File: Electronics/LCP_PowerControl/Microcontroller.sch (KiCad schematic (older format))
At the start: 20 parts, among them J4 Conn_02x02_Odd_Even, J5 Conn_02x05_Odd_Even, J6 Conn_02x06_Odd_Even, J7 Conn_02x02_Odd_Even, J8 Conn_02x02_Odd_Even, SW1 SW_Push, U3 MSP430FR5989, Y1 32.768kHz

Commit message: Adding libraries and recent changes
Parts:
- added RN? (x2): R_Pack02, symbol Device:R_Pack02
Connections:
- net +3V3: now also RN?.3 (R2.2), RN?.3 (R2.2), RN?.4 (R1.2), RN?.4 (R1.2)
- net BM_SCL: now also RN?.2 (R2.1)
- net BM_SDA: now also RN?.1 (R1.1)
- net CONTROL_SCL: now also RN?.2 (R2.1)
- net CONTROL_SDA: now also RN?.1 (R1.1)
- net HALL_EFFECT_CH_A renamed ENCODER_CH_A
- net HALL_EFFECT_CH_B renamed ENCODER_CH_B
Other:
- moved on the sheet: C10, C11, C12, C13, C14, C15, C16, C8, C9, J5, J6, JP1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

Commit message: Aiming for rev 0.1 complete
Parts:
- C16: value 1n -> 1000pF; footprint (none) -> Capacitor_SMD:C_0603_1608Metric
- J4, J7, J8: footprint (none) -> Connector_PinHeader_2.00mm:PinHeader_2x02_P2.00mm_Vertical
- J5: footprint (none) -> Connector_PinSocket_1.27mm:PinSocket_2x05_P1.27mm_Vertical
- J6: footprint (none) -> Connector_PinHeader_2.00mm:PinHeader_2x06_P2.00mm_Vertical
- JP1, JP2: footprint (none) -> Jumper:SolderJumper-2_P1.3mm_Bridged_RoundedPad1.0x1.5mm
- R13: footprint (none) -> Resistor_SMD:R_0805_2012Metric
- RN1, RN2: renamed from RN?; footprint (none) -> Resistor_SMD:R_Array_Concave_2x0603; MPN (none) -> EXB-V4V472JV
- SW1: footprint (none) -> Button_Switch_SMD:SW_SPST_TL3305A; MPN (none) -> PTS810 SJS 250 SMTR LFS
- Y1: footprint (none) -> Crystal:Crystal_SMD_HC49-SD
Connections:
- net P5.3: now reaches U3.13 (P5.3/UDB1STE)
- net P1.4: now reaches U3.2 (P1.4/UCB0CLK/UCA0STE/TA1.0)
- net P3.3: now reaches U3.25 (P3.3/TA1.1/TB0CLK)
- net P2.3: now reaches U3.30 (P2.3/UCA0STE/TB0OUTH)
- net P2.2: now reaches U3.31 (P2.2/UCA0CLK/TB0.4/RTCCLK)
- net P1.3: now reaches U3.36 (P1.3/ESITEST4/TA1.2/A3/C3)
- net P2.6: now reaches U3.8 (P2.6/TB0.5/ESIC1OUT)
- net P2.7: now reaches U3.9 (P2.7/TB0.6/ESIC2OUT)
- no-connect marks 8 -> 13
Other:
- note added: "Unused Nets"
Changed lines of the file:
@@
 Sheet 8 11
 Title ""
-Date ""
-Rev ""
+Date "2020-06-17"
+Rev "R0.1"
 Comp ""
-Comment1 ""
+Comment1 "Design by: Matt Casari"
 Comment2 ""
 Comment3 ""
@@
 Text HLabel 15050 4000 2    50   Output ~ 0
 ~MD_SLEEP
-Text HLabel 3900 8550 0    50   Output ~ 0
+Text HLabel 3900 5550 0    50   Output ~ 0
 12V_ENABLE
 $Comp
@@
 U 1 1 5EE55967
 P 8300 4750
-F 0 "U3" H 8275 7281 50  0000 C CNN
-F 1 "MSP430FR5989" H 8275 7190 50  0000 C CNN
+F 0 "U3" H 9750 7050 50  0000 C CNN
+F 1 "MSP430FR5989" H 7100 7050 50  0000 C CNN
 F 2 "Package_QFP:LQFP-64_10x10mm_P0.5mm" H 7700 6450 50  0001 C CNN
 F 3 "https://www.ti.com/lit/ds/symlink/msp430fr5989.pdf?ts=1591995725922&ref_url=https%253A%252F%252Fwww.ti.com%252Fproduct%252FMSP430FR5989" H 7700 6450 50  0001 C CNN
@@
 F 0 "JP1" H 8300 7400 50  0000 C CNN
 F 1 "SolderJumper_2_Bridged" H 8300 7000 50  0001 C CNN
-F 2 "" H 8300 7300 50  0001 C CNN
+F 2 "Jumper:SolderJumper-2_P1.3mm_Bridged_RoundedPad1.0x1.5mm" H 8300 7300 50  0001 C CNN
 F 3 "~" H 8300 7300 50  0001 C CNN
 	1    8300 7300
@@
 F 0 "J5" V 11459 2580 50  0000 L CNN
 F 1 "Conn_02x05_Odd_Even" V 11550 2580 50  0000 L CNN
-F 2 "" H 11500 2300 50  0001 C CNN
+F 2 "Connector_PinSocket_1.27mm:PinSocket_2x05_P1.27mm_Vertical" H 11500 2300 50  0001 C CNN
 F 3 "~" H 11500 2300 50  0001 C CNN
 F 4 "JTAG_MINI" V 11641 2580 50  0000 L CNN "Field4"
@@
 F 0 "Y1" V 10054 6631 50  0000 L CNN
 F 1 "32.768kHz" V 10145 6631 50  0000 L CNN
-F 2 "" H 10100 6500 50  0001 C CNN
+F 2 "Crystal:Crystal_SMD_HC49-SD" H 10100 6500 50  0001 C CNN
 F 3 "~" H 10100 6500 50  0001 C CNN
 	1    10100 6500
@@
 F 0 "R13" H 12220 3346 50  0000 L CNN
 F 1 "470" H 12220 3255 50  0000 L CNN
-F 2 "" V 12080 3300 50  0001 C CNN
+F 2 "Resistor_SMD:R_0805_2012Metric" V 12080 3300 50  0001 C CNN
 F 3 "~" H 12150 3300 50  0001 C CNN
 	1    12150 3300
@@
 P 12150 3700
 F 0 "C16" H 12265 3746 50  0000 L CNN
-F 1 "1n" H 12265 3655 50  0000 L CNN
-F 2 "" H 12188 3550 50  0001 C CNN
+F 1 "1000pF" H 12265 3655 50  0000 L CNN
+F 2 "Capacitor_SMD:C_0603_1608Metric" H 12188 3550 50  0001 C CNN
 F 3 "~" H 12150 3700 50  0001 C CNN
 	1    12150 3700
@@
 F 0 "SW1" H 12650 3785 50  0000 C CNN
 F 1 "SW_Push" H 12650 3694 50  0000 C CNN
-F 2 "" H 12650 3700 50  0001 C CNN
+F 2 "Button_Switch_SMD:SW_SPST_TL3305A" H 12650 3700 50  0001 C CNN
 F 3 "~" H 12650 3700 50  0001 C CNN
+F 4 "PTS810 SJS 250 SMTR LFS" H 12650 3500 50  0001 C CNN "MPN"
 	1    12650 3500
 	1    0    0    -1
@@
 F 0 "JP2" V 8600 2050 50  0000 L CNN
 F 1 "SolderJumper_2_Bridged" V 8745 2268 50  0001 L CNN
-F 2 "" H 8700 2200 50  0001 C CNN
+F 2 "Jumper:SolderJumper-2_P1.3mm_Bridged_RoundedPad1.0x1.5mm" H 8700 2200 50  0001 C CNN
 F 3 "~" H 8700 2200 50  0001 C CNN
 	1    8700 2200
@@
 Wire Wire Line
 	6200 5500 6650 5500
-NoConn ~ 9900 3950
-NoConn ~ 9900 4050
 Wire Wire Line
 	13850 4350 13950 4350
@@
 F 0 "J4" V 13946 4562 50  0000 R CNN
 F 1 "Conn_02x02_Odd_Even" V 13855 4562 50  0000 R CNN
-F 2 "" H 13850 4750 50  0001 C CNN
+F 2 "Connector_PinHeader_2.00mm:PinHeader_2x02_P2.00mm_Vertical" H 13850 4750 50  0001 C CNN
 F 3 "~" H 13850 4750 50  0001 C CNN
 	1    13850 4750
@@
 Wire Wire Line
 	14750 4200 15050 4200
-NoConn ~ 9900 4150
-NoConn ~ 6650 5800
-NoConn ~ 6650 4700
-NoConn ~ 6650 4600
 Text GLabel 14750 4300 0    50   BiDi ~ 0
 P5.1
@@
 F 0 "J6" H 12750 8350 50  0000 C CNN
 F 1 "Conn_02x06_Odd_Even" H 12750 7650 50  0000 C CNN
-F 2 "" H 12700 8050 50  0001 C CNN
+F 2 "Connector_PinHeader_2.00mm:PinHeader_2x06_P2.00mm_Vertical" H 12700 8050 50  0001 C CNN
 F 3 "~" H 12700 8050 50  0001 C CNN
 	1    12700 8050
@@
 F 0 "J7" H 14250 6250 50  0000 C CNN
 F 1 "Conn_02x02_Odd_Even" H 14250 5950 50  0000 C CNN
-F 2 "" H 14200 6150 50  0001 C CNN
+F 2 "Connector_PinHeader_2.00mm:PinHeader_2x02_P2.00mm_Vertical" H 14200 6150 50  0001 C CNN
 F 3 "~" H 14200 6150 50  0001 C CNN
 	1    14200 6150
@@
 F 0 "J8" H 14250 6750 50  0000 C CNN
 F 1 "Conn_02x02_Odd_Even" H 14250 6450 50  0000 C CNN
-F 2 "" H 14200 6650 50  0001 C CNN
+F 2 "Connector_PinHeader_2.00mm:PinHeader_2x02_P2.00mm_Vertical" H 14200 6650 50  0001 C CNN
 F 3 "~" H 14200 6650 50  0001 C CNN
 	1    14200 6650
@@
 Wire Wire Line
 	13850 6750 14000 6750
-Text GLabel 4350 8550 2    50   Input ~ 0
+Text GLabel 4350 5550 2    50   Input ~ 0
 P2.5
 Wire Wire Line
-	3900 8550 4350 8550
+	3900 5550 4350 5550
 Wire Wire Line
 	9900 3500 11300 3500
 $Comp
-L Device:R_Pack02 RN?
+L Device:R_Pack02 RN1
 U 1 1 5EEA03AB
 P 4350 2450
-F 0 "RN?" H 4438 2496 50  0000 L CNN
+F 0 "RN1" H 4438 2496 50  0000 L CNN
 F 1 "R_Pack02" H 4438 2405 50  0000 L CNN
-F 2 "" V 4525 2450 50  0001 C CNN
+F 2 "Resistor_SMD:R_Array_Concave_2x0603" V 4525 2450 50  0001 C CNN
 F 3 "~" H 4350 2450 50  0001 C CNN
+F 4 "EXB-V4V472JV" H 4350 2450 50  0001 C CNN "MPN"
 	1    4350 2450
 	1    0    0    -1
 $EndComp
 $Comp
-L Device:R_Pack02 RN?
+L Device:R_Pack02 RN2
 U 1 1 5EEA12D1
 P 5050 2450
-F 0 "RN?" H 5138 2496 50  0000 L CNN
+F 0 "RN2" H 5138 2496 50  0000 L CNN
 F 1 "R_Pack02" H 5138 2405 50  0000 L CNN
-F 2 "" V 5225 2450 50  0001 C CNN
+F 2 "Resistor_SMD:R_Array_Concave_2x0603" V 5225 2450 50  0001 C CNN
 F 3 "~" H 5050 2450 50  0001 C CNN
+F 4 "EXB-V4V472JV" H 5050 2450 50  0001 C CNN "MPN"
 	1    5050 2450
 	1    0    0    -1
 $EndComp
 $Comp
-L power:+3V3 #PWR?
+L power:+3V3 #PWR059
 U 1 1 5EEA1A6A
 P 4250 2100
-F 0 "#PWR?" H 4250 1950 50  0001 C CNN
+F 0 "#PWR059" H 4250 1950 50  0001 C CNN
 F 1 "+3V3" H 4265 2273 50  0000 C CNN
 F 2 "" H 4250 2100 50  0001 C CNN
@@
 Wire Wire Line
 	5050 3800 3900 3800
+Text GLabel 7250 8750 0    50   BiDi ~ 0
+P4.0
+Text GLabel 7250 8850 0    50   BiDi ~ 0
+P4.1
+Text GLabel 7250 8950 0    50   BiDi ~ 0
+P5.2
+Text GLabel 6500 2950 0    50   BiDi ~ 0
+P1.4
+Wire Wire Line
+	6500 2950 6650 2950
+Text GLabel 6500 3500 0    50   BiDi ~ 0
+P5.3
+Wire Wire Line
+	6500 3500 6650 3500
+Text GLabel 7250 9050 0    50   BiDi ~ 0
+P5.3
+Text GLabel 6500 8750 0    50   BiDi ~ 0
+P1.4
+Text GLabel 10150 3950 2    50   BiDi ~ 0
+P2.6
+Text GLabel 10150 4050 2    50   BiDi ~ 0
+P2.7
+Text GLabel 10150 4150 2    50   BiDi ~ 0
+P1.3
+Wire Wire Line
+	10150 4150 9900 4150
+Wire Wire Line
+	9900 4050 10150 4050
+Wire Wire Line
+	10150 3950 9900 3950
+Text GLabel 6500 9050 0    50   BiDi ~ 0
+P2.6
+Text GLabel 6500 9150 0    50   BiDi ~ 0
+P2.7
+Text GLabel 6500 8650 0    50   BiDi ~ 0
+P1.3
+Text GLabel 6450 4700 0    50   BiDi ~ 0
+P2.2
+Text GLabel 6450 4600 0    50   BiDi ~ 0
+P2.3
+Wire Wire Line
+	6650 4600 6450 4600
+Wire Wire Line
+	6650 4700 6450 4700
+Text GLabel 6500 8850 0    50   BiDi ~ 0
+P2.2
+Text GLabel 6500 8950 0    50   BiDi ~ 0
+P2.3
+Text GLabel 6200 5800 0    50   BiDi ~ 0
+P3.3
+Wire Wire Line
+	6650 5800 6200 5800
+Text GLabel 7250 8650 0    50   BiDi ~ 0
+P3.3
+NoConn ~ 6500 8650
+NoConn ~ 6500 8750
+NoConn ~ 6500 8850
+NoConn ~ 6500 8950
+NoConn ~ 6500 9050
+NoConn ~ 6500 9150
+NoConn ~ 7250 9050
+NoConn ~ 7250 8950
+NoConn ~ 7250 8850
+NoConn ~ 7250 8750
+NoConn ~ 7250 8650
+Text Notes 6400 8450 0    100  ~ 0
+Unused Nets
+$Comp
+L power:PWR_FLAG #FLG0106
+U 1 1 5F032956
+P 8450 1750
+F 0 "#FLG0106" H 8450 1825 50  0001 C CNN
+F 1 "PWR_FLAG" H 8450 1923 50  0000 C CNN
+F 2 "" H 8450 1750 50  0001 C CNN
+F 3 "~" H 8450 1750 50  0001 C CNN
+	1    8450 1750
+	1    0    0    -1
+$EndComp
+Wire Wire Line
+	8450 1750 8450 2350
+Wire Wire Line
+	8450 2350 8700 2350
+Connection ~ 8700 2350
+$Comp
+L power:PWR_FLAG #FLG0107
+U 1 1 5F03FA58
+P 8950 7250
+F 0 "#FLG0107" H 8950 7325 50  0001 C CNN
+F 1 "PWR_FLAG" H 8950 7423 50  0000 C CNN
+F 2 "" H 8950 7250 50  0001 C CNN
+F 3 "~" H 8950 7250 50  0001 C CNN
+	1    8950 7250
+	1    0    0    -1
+$EndComp
+Wire Wire Line
+	8950 7250 8950 7300
+Wire Wire Line
+	8950 7300 8750 7300
+Connection ~ 8750 7300
 $EndSCHEMATC

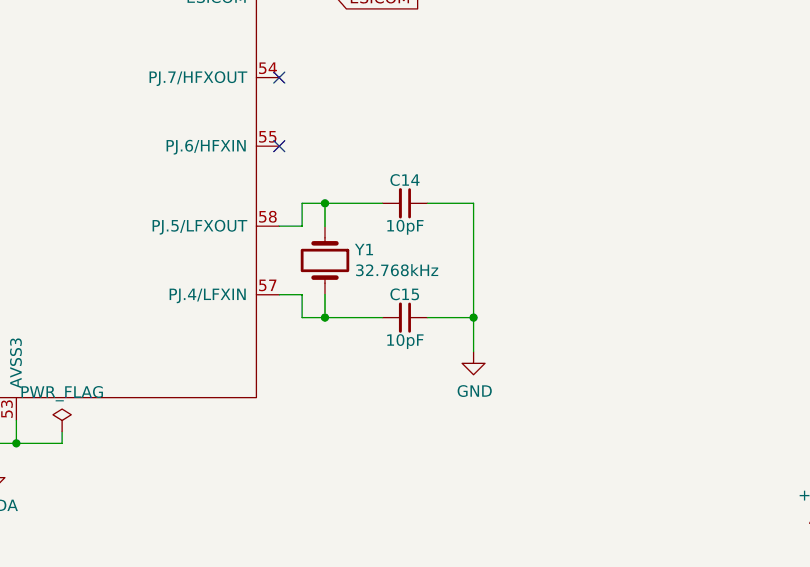
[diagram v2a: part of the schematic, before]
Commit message: KiCad Layout
Component and Traces finished. Need a look over. Will work on Silkscreen
after.

JTAG Connector. Should pin 1 be pulled up w/ 470Ohm resistor similar to
other designs? Also TDI and TMI signals are connected, is this correct?
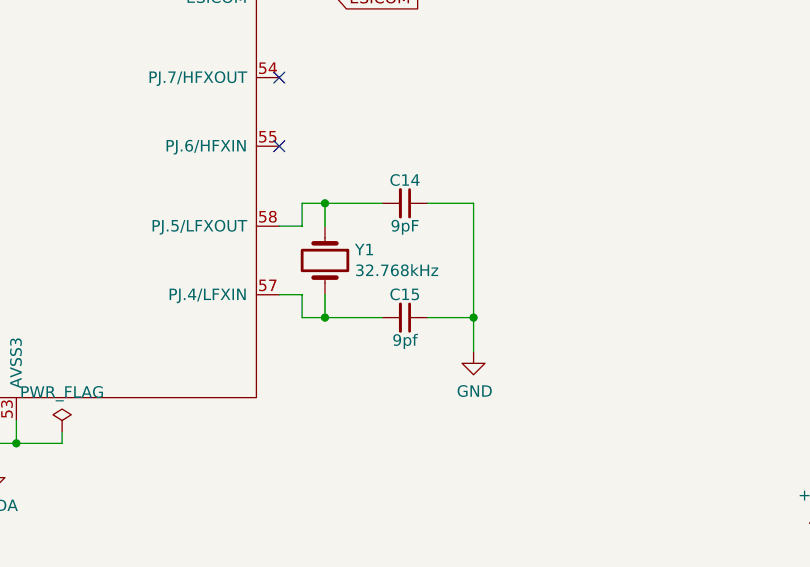
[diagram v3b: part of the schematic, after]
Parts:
- C14: value 10pF -> 9pF; MPN (none) -> CBR06C909B5GAC
- C15: value 10pF -> 9pf; MPN (none) -> CBR06C909B5GAC
- C8: MPN (none) -> EEE-HB1C100R
- Y1: footprint Crystal:Crystal_SMD_HC49-SD -> Crystal:Crystal_SMD_3215-2Pin_3.2x1.5mm; Field4 (none) -> ABS07-32.768KHZ-9-T
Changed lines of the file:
@@
 	9900 3200 11700 3200
-Wire Wire Line
-	11700 3200 11700 3100
 Wire Wire Line
 	9900 3300 11600 3300
@@
 Wire Wire Line
 	10850 1950 11400 1950
-Connection ~ 11400 3100
-Wire Wire Line
-	11400 3100 11700 3100
-Connection ~ 11700 3100
-Wire Wire Line
-	11700 3100 11700 2600
 $Comp
 L power:+3V3 #PWR019
@@
 F 2 "Capacitor_SMD:CP_Elec_4x4.5" H 6188 1950 50  0001 C CNN
 F 3 "~" H 6150 2100 50  0001 C CNN
+F 4 "EEE-HB1C100R" H 6150 2100 50  0001 C CNN "MPN"
 	1    6150 2100
 	1    0    0    -1
@@
 F 0 "Y1" V 10054 6631 50  0000 L CNN
 F 1 "32.768kHz" V 10145 6631 50  0000 L CNN
-F 2 "Crystal:Crystal_SMD_HC49-SD" H 10100 6500 50  0001 C CNN
+F 2 "Crystal:Crystal_SMD_3215-2Pin_3.2x1.5mm" H 10100 6500 50  0001 C CNN
 F 3 "~" H 10100 6500 50  0001 C CNN
+F 4 "ABS07-32.768KHZ-9-T" V 10100 6500 50  0001 C CNN "Field4"
 	1    10100 6500
 	0    1    1    0
@@
 P 10450 6250
 F 0 "C14" V 10350 6250 50  0000 C CNN
-F 1 "10pF" V 10550 6250 50  0000 C CNN
+F 1 "9pF" V 10550 6250 50  0000 C CNN
 F 2 "Capacitor_SMD:C_0603_1608Metric" H 10450 6250 50  0001 C CNN
 F 3 "~" H 10450 6250 50  0001 C CNN
+F 4 "CBR06C909B5GAC" V 10450 6250 50  0001 C CNN "MPN"
 	1    10450 6250
 	0    1    1    0
@@
 P 10450 6750
 F 0 "C15" V 10350 6750 50  0000 C CNN
-F 1 "10pF" V 10550 6750 50  0000 C CNN
+F 1 "9pf" V 10550 6750 50  0000 C CNN
 F 2 "Capacitor_SMD:C_0603_1608Metric" H 10450 6750 50  0001 C CNN
 F 3 "~" H 10450 6750 50  0001 C CNN
+F 4 "CBR06C909B5GAC" V 10450 6750 50  0001 C CNN "MPN"
 	1    10450 6750
 	0    1    1    0
@@
 	8950 7300 8750 7300
 Connection ~ 8750 7300
+Wire Wire Line
+	11700 3100 11700 2600
+Wire Wire Line
+	11700 3200 11700 3100
+Connection ~ 11700 3100
+Connection ~ 11400 3100
+Wire Wire Line
+	11400 3100 11700 3100
 $EndSCHEMATC

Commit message: LCP_PowerControl Rev1
Board layout in Kicad.
Gerbers.
BOM
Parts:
- C10, C11, C12, C13, C9: MPN (none) -> 885012207045
- C16: MPN (none) -> GCJ188R72A102KA01D
- R13: MPN (none) -> CRGCQ0805F470R
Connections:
- net BM_SDA: no longer U3.4 (P1.6/USB0SIMO/UCB0SDA/TA0.1)
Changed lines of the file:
@@
 F 2 "Capacitor_SMD:C_0805_2012Metric" H 7588 1950 50  0001 C CNN
 F 3 "~" H 7550 2100 50  0001 C CNN
+F 4 "885012207045" H 7550 2100 50  0001 C CNN "MPN"
 	1    7550 2100
 	1    0    0    -1
@@
 F 2 "Capacitor_SMD:C_0805_2012Metric" H 6638 1950 50  0001 C CNN
 F 3 "~" H 6600 2100 50  0001 C CNN
+F 4 "885012207045" H 6600 2100 50  0001 C CNN "MPN"
 	1    6600 2100
 	1    0    0    -1
@@
 F 2 "Capacitor_SMD:C_0805_2012Metric" H 7088 1950 50  0001 C CNN
 F 3 "~" H 7050 2100 50  0001 C CNN
+F 4 "885012207045" H 7050 2100 50  0001 C CNN "MPN"
 	1    7050 2100
 	1    0    0    -1
@@
 F 2 "Capacitor_SMD:C_0805_2012Metric" H 9538 1950 50  0001 C CNN
 F 3 "~" H 9500 2100 50  0001 C CNN
+F 4 "885012207045" H 9500 2100 50  0001 C CNN "MPN"
 	1    9500 2100
 	1    0    0    -1
@@
 F 2 "Capacitor_SMD:C_0805_2012Metric" H 9088 1950 50  0001 C CNN
 F 3 "~" H 9050 2100 50  0001 C CNN
+F 4 "885012207045" H 9050 2100 50  0001 C CNN "MPN"
 	1    9050 2100
 	1    0    0    -1
@@
 F 2 "Resistor_SMD:R_0805_2012Metric" V 12080 3300 50  0001 C CNN
 F 3 "~" H 12150 3300 50  0001 C CNN
+F 4 "CRGCQ0805F470R" H 12150 3300 50  0001 C CNN "MPN"
 	1    12150 3300
 	1    0    0    -1
@@
 F 2 "Capacitor_SMD:C_0603_1608Metric" H 12188 3550 50  0001 C CNN
 F 3 "~" H 12150 3700 50  0001 C CNN
+F 4 "GCJ188R72A102KA01D" H 12150 3700 50  0001 C CNN "MPN"
 	1    12150 3700
 	1    0    0    -1
@@
 Wire Wire Line
 	4250 2650 4250 3150
-Connection ~ 4250 3150
-Wire Wire Line
-	4250 3150 6650 3150
 Wire Wire Line
 	4350 2650 4350 3250
